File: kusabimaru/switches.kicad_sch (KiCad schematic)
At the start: 148 parts

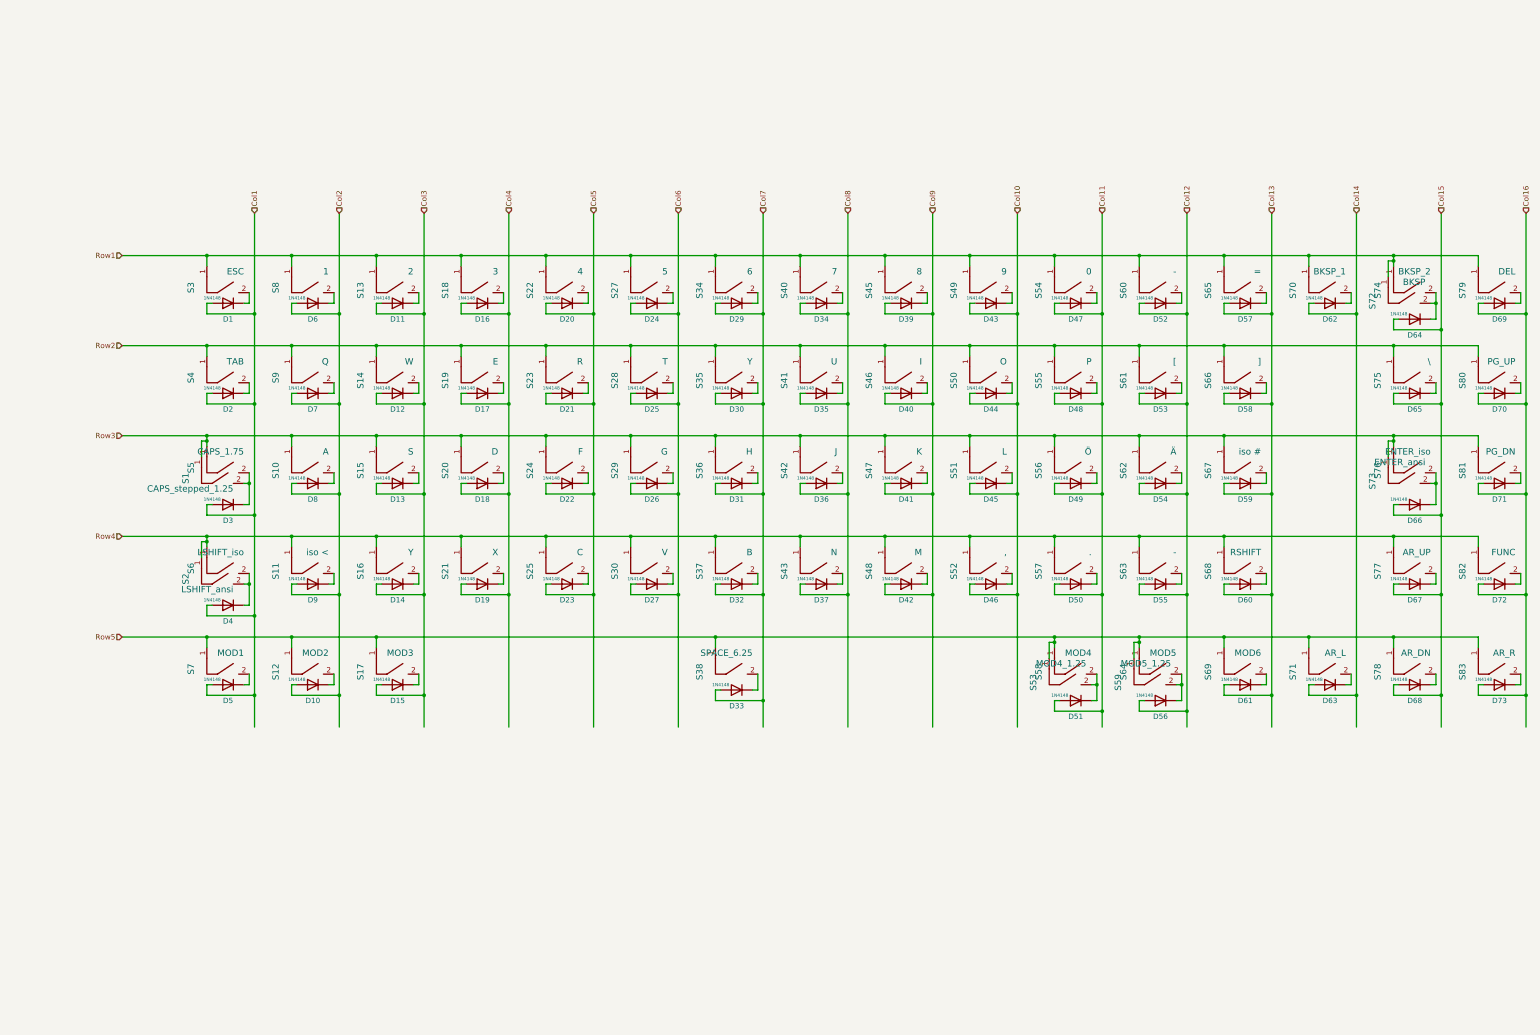
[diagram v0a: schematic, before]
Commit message: Changed schematic and PCB layout for kuro65. Routing of PCB is incomplete.
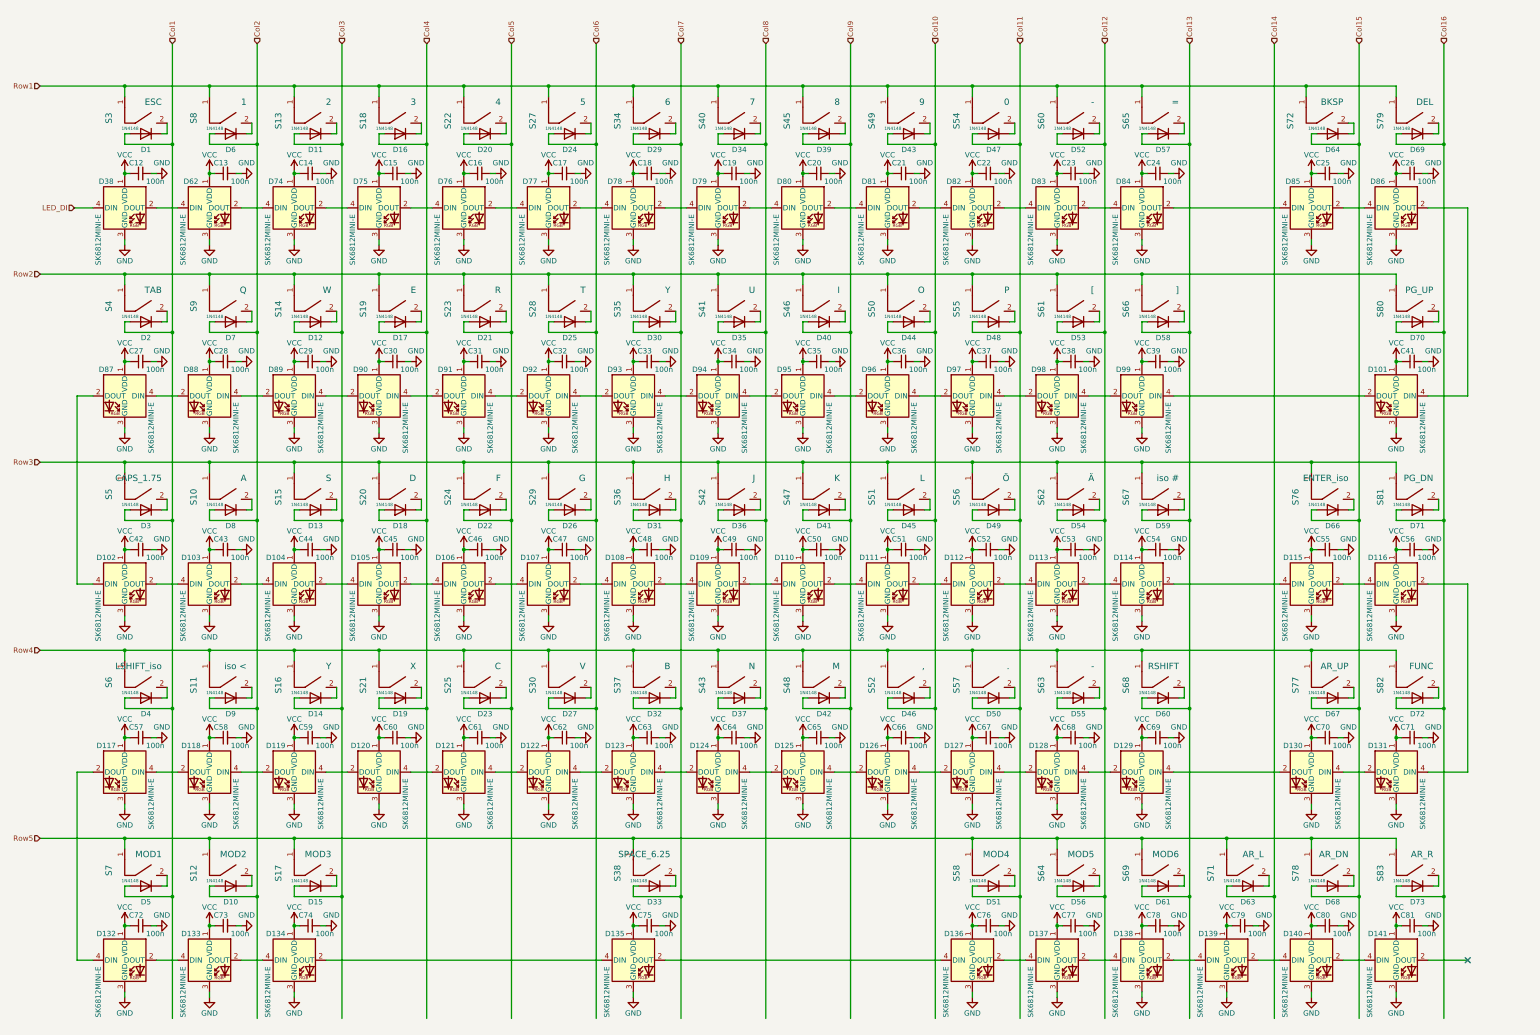
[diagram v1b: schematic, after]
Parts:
- removed D62, D65: 1N4148, Diode_SMD:D_SOD-323_HandSoldering, symbol Device:D
- removed S1: CAPS_stepped_1.25, keyswitches:Kailh_socket_only_MX_1.25u, symbol mx1a-simple:MX1A
- removed S2: LSHIFT_ansi, keyswitches:Kailh_socket_only_MX_2.25u, symbol mx1a-simple:MX1A
- removed S53: MOD4_1.25, keyswitches:Kailh_socket_only_MX_1.25u, symbol mx1a-simple:MX1A
- removed S59: MOD5_1.25, keyswitches:Kailh_socket_only_MX_1.25u, symbol mx1a-simple:MX1A
- removed S70: BKSP_1, keyswitches:Kailh_socket_only_MX_1u, symbol mx1a-simple:MX1A
- removed S73: ENTER_ansi, keyswitches:Kailh_socket_only_MX_2.25u, symbol mx1a-simple:MX1A
- removed S74: BKSP_2, keyswitches:Kailh_socket_only_MX_1u, symbol mx1a-simple:MX1A
- removed S75: \, keyswitches:Kailh_socket_only_MX_1.5u, symbol mx1a-simple:MX1A
- added C12, C13, C14, C15, C16, C17, C18, C19, C20, C21, C22, C23, C24, C25, C26, C27, C28, C29, C30, C31, C32, C33, C34, C35, C36, C37, C38, C39, C41, C42, C43, C44, C45, C46, C47, C48, C49, C50, C51, C52, C53, C54, C55, C56, C57, C58, C59, C60, C61, C62, C63, C64, C65, C66, C67, C68, C69, C70, C71, C72, C73, C74, C75, C76, C77, C78, C79, C80, C81: 100n, Capacitor_SMD:C_0603_1608Metric_Pad1.08x0.95mm_HandSolder, symbol Device:C_Small
- added D101, D102, D103, D104, D105, D106, D107, D108, D109, D110, D111, D112, D113, D114, D115, D116, D117, D118, D119, D120, D121, D122, D123, D124, D125, D126, D127, D128, D129, D130, D131, D132, D133, D134, D135, D136, D137, D138, D139, D140, D141, D38, D62, D74, D75, D76, D77, D78, D79, D80, D81, D82, D83, D84, D85, D86, D87, D88, D89, D90, D91, D92, D93, D94, D95, D96, D97, D98, D99: SK6812MINI-E, TM_leds:SK6812_MINI_E_small_cutout, symbol tm_leds:SK6812MINI-E
- D1, D10, D11, D12, D13, D14, D15, D16, D17, D18, D19, D2, D20, D21, D22, D23, D24, D25, D26, D27, D29, D3, D30, D31, D32, D33, D34, D35, D36, D37, D39, D4, D40, D41, D42, D43, D44, D45, D46, D47, D48, D49, D5, D50, D51, D52, D53, D54, D55, D56, D57, D58, D59, D6, D60, D61, D63, D64, D66, D67, D68, D69, D7, D70, D71, D72, D73, D8, D9: footprint Diode_SMD:D_SOD-323_HandSoldering -> Diode_SMD:D_SOD-123
- S10, S11, S13, S14, S15, S16, S18, S19, S20, S21, S22, S23, S24, S25, S27, S28, S29, S30, S34, S35, S36, S37, S40, S41, S42, S43, S45, S46, S47, S48, S49, S50, S51, S52, S54, S55, S56, S57, S58, S60, S61, S62, S63, S64, S65, S66, S67, S69, S71, S77, S78, S79, S80, S81, S82, S83, S9: footprint keyswitches:Kailh_socket_only_MX_1u -> keyswitches:Kailh_socket_only_MX_smd_1u
- S3, S8: footprint keyswitches:Kailh_socket_MX_1u -> keyswitches:Kailh_socket_only_MX_smd_1u
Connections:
- new net: D84.2 (DOUT), D85.4 (DIN)
- new net: D83.2 (DOUT), D84.4 (DIN)
- new net: D140.2 (DOUT), D141.4 (DIN)
- new net: D139.2 (DOUT), D140.4 (DIN)
- new net: D80.2 (DOUT), D81.4 (DIN)
- new net: D79.2 (DOUT), D80.4 (DIN)
- new net: D91.4 (DIN), D92.2 (DOUT)
- new net: D92.4 (DIN), D93.2 (DOUT)
- new net: D78.2 (DOUT), D79.4 (DIN)
- new net: D76.2 (DOUT), D77.4 (DIN)
- new net: D75.2 (DOUT), D76.4 (DIN)
- new net: D74.2 (DOUT), D75.4 (DIN)
- new net: D62.2 (DOUT), D74.4 (DIN)
- new net: D77.2 (DOUT), D78.4 (DIN)
- new net: D82.2 (DOUT), D83.4 (DIN)
- new net: D111.2 (DOUT), D112.4 (DIN)
- new net: D110.2 (DOUT), D111.4 (DIN)
- new net: D95.4 (DIN), D96.2 (DOUT)
- new net: D96.4 (DIN), D97.2 (DOUT)
- new net: D81.2 (DOUT), D82.4 (DIN)
- new net: D127.4 (DIN), D128.2 (DOUT)
- new net: D128.4 (DIN), D129.2 (DOUT)
- new net: D89.4 (DIN), D90.2 (DOUT)
- new net: D90.4 (DIN), D91.2 (DOUT)
- new net: D87.4 (DIN), D88.2 (DOUT)
- new net: D88.4 (DIN), D89.2 (DOUT)
- new net: D117.4 (DIN), D118.2 (DOUT)
- new net: D118.4 (DIN), D119.2 (DOUT)
- new net: D130.4 (DIN), D131.2 (DOUT)
- new net: D116.2 (DOUT), D131.4 (DIN)
- new net: D108.2 (DOUT), D109.4 (DIN)
- new net: D107.2 (DOUT), D108.4 (DIN)
- new net: D109.2 (DOUT), D110.4 (DIN)
- new net: D101.2 (DOUT), D99.4 (DIN)
- new net: D101.4 (DIN), D86.2 (DOUT)
- new net: D106.2 (DOUT), D107.4 (DIN)
- new net: D85.2 (DOUT), D86.4 (DIN)
- new net: D126.4 (DIN), D127.2 (DOUT)
- new net: D105.2 (DOUT), D106.4 (DIN)
- new net: D135.2 (DOUT), D136.4 (DIN)
- new net: D134.2 (DOUT), D135.4 (DIN)
- new net: D114.2 (DOUT), D115.4 (DIN)
- new net: D113.2 (DOUT), D114.4 (DIN)
- new net: D125.4 (DIN), D126.2 (DOUT)
- new net: D137.2 (DOUT), D138.4 (DIN)
- new net: D136.2 (DOUT), D137.4 (DIN)
- new net: D138.2 (DOUT), D139.4 (DIN)
- new net: D121.4 (DIN), D122.2 (DOUT)
- new net: D122.4 (DIN), D123.2 (DOUT)
- new net: D112.2 (DOUT), D113.4 (DIN)
- new net: D104.2 (DOUT), D105.4 (DIN)
- new net: D103.2 (DOUT), D104.4 (DIN)
- new net: D97.4 (DIN), D98.2 (DOUT)
- new net: D98.4 (DIN), D99.2 (DOUT)
- new net: D115.2 (DOUT), D116.4 (DIN)
- new net: D119.4 (DIN), D120.2 (DOUT)
- new net: D120.4 (DIN), D121.2 (DOUT)
- new net: D133.2 (DOUT), D134.4 (DIN)
- new net: D132.2 (DOUT), D133.4 (DIN)
- new net: D102.4 (DIN), D87.2 (DOUT)
- new net: D94.4 (DIN), D95.2 (DOUT)
- new net: D129.4 (DIN), D130.2 (DOUT)
- new net: D38.2 (DOUT), D62.4 (DIN)
- new net: D102.2 (DOUT), D103.4 (DIN)
- new net: D117.2 (DOUT), D132.4 (DIN)
- new net: D123.4 (DIN), D124.2 (DOUT)
- new net: D93.4 (DIN), D94.2 (DOUT)
- new net: D124.4 (DIN), D125.2 (DOUT)
- new net GND: C12.2, C13.2, C14.2, C15.2, C16.2, C17.2, C18.2, C19.2, C20.2, C21.2, C22.2, C23.2, C24.2, C25.2, C26.2, C27.2, C28.2, C29.2, C30.2, C31.2, C32.2, C33.2, C34.2, C35.2, C36.2, C37.2, C38.2, C39.2, C41.2, C42.2, C43.2, C44.2, C45.2, C46.2, C47.2, C48.2, C49.2, C50.2, C51.2, C52.2, C53.2, C54.2, C55.2, C56.2, C57.2, C58.2, C59.2, C60.2, C61.2, C62.2, C63.2, C64.2, C65.2, C66.2, C67.2, C68.2, C69.2, C70.2, C71.2, C72.2, C73.2, C74.2, C75.2, C76.2, C77.2, C78.2, C79.2, C80.2, C81.2, D101.3 (GND), D102.3 (GND), D103.3 (GND), D104.3 (GND), D105.3 (GND), D106.3 (GND), D107.3 (GND), D108.3 (GND), D109.3 (GND), D110.3 (GND), D111.3 (GND), D112.3 (GND), D113.3 (GND), D114.3 (GND), D115.3 (GND), D116.3 (GND), D117.3 (GND), D118.3 (GND), D119.3 (GND), D120.3 (GND), D121.3 (GND), D122.3 (GND), D123.3 (GND), D124.3 (GND), D125.3 (GND), D126.3 (GND), D127.3 (GND), D128.3 (GND), D129.3 (GND), D130.3 (GND), D131.3 (GND), D132.3 (GND), D133.3 (GND), D134.3 (GND), D135.3 (GND), D136.3 (GND), D137.3 (GND), D138.3 (GND), D139.3 (GND), D140.3 (GND), D141.3 (GND), D38.3 (GND), D62.3 (GND), D74.3 (GND), D75.3 (GND), D76.3 (GND), D77.3 (GND), D78.3 (GND), D79.3 (GND), D80.3 (GND), D81.3 (GND), D82.3 (GND), D83.3 (GND), D84.3 (GND), D85.3 (GND), D86.3 (GND), D87.3 (GND), D88.3 (GND), D89.3 (GND), D90.3 (GND), D91.3 (GND), D92.3 (GND), D93.3 (GND), D94.3 (GND), D95.3 (GND), D96.3 (GND), D97.3 (GND), D98.3 (GND), D99.3 (GND)
- new net LED_DI: D38.4 (DIN)
- new net VCC: C12.1, C13.1, C14.1, C15.1, C16.1, C17.1, C18.1, C19.1, C20.1, C21.1, C22.1, C23.1, C24.1, C25.1, C26.1, C27.1, C28.1, C29.1, C30.1, C31.1, C32.1, C33.1, C34.1, C35.1, C36.1, C37.1, C38.1, C39.1, C41.1, C42.1, C43.1, C44.1, C45.1, C46.1, C47.1, C48.1, C49.1, C50.1, C51.1, C52.1, C53.1, C54.1, C55.1, C56.1, C57.1, C58.1, C59.1, C60.1, C61.1, C62.1, C63.1, C64.1, C65.1, C66.1, C67.1, C68.1, C69.1, C70.1, C71.1, C72.1, C73.1, C74.1, C75.1, C76.1, C77.1, C78.1, C79.1, C80.1, C81.1, D101.1 (VDD), D102.1 (VDD), D103.1 (VDD), D104.1 (VDD), D105.1 (VDD), D106.1 (VDD), D107.1 (VDD), D108.1 (VDD), D109.1 (VDD), D110.1 (VDD), D111.1 (VDD), D112.1 (VDD), D113.1 (VDD), D114.1 (VDD), D115.1 (VDD), D116.1 (VDD), D117.1 (VDD), D118.1 (VDD), D119.1 (VDD), D120.1 (VDD), D121.1 (VDD), D122.1 (VDD), D123.1 (VDD), D124.1 (VDD), D125.1 (VDD), D126.1 (VDD), D127.1 (VDD), D128.1 (VDD), D129.1 (VDD), D130.1 (VDD), D131.1 (VDD), D132.1 (VDD), D133.1 (VDD), D134.1 (VDD), D135.1 (VDD), D136.1 (VDD), D137.1 (VDD), D138.1 (VDD), D139.1 (VDD), D140.1 (VDD), D141.1 (VDD), D38.1 (VDD), D62.1 (VDD), D74.1 (VDD), D75.1 (VDD), D76.1 (VDD), D77.1 (VDD), D78.1 (VDD), D79.1 (VDD), D80.1 (VDD), D81.1 (VDD), D82.1 (VDD), D83.1 (VDD), D84.1 (VDD), D85.1 (VDD), D86.1 (VDD), D87.1 (VDD), D88.1 (VDD), D89.1 (VDD), D90.1 (VDD), D91.1 (VDD), D92.1 (VDD), D93.1 (VDD), D94.1 (VDD), D95.1 (VDD), D96.1 (VDD), D97.1 (VDD), D98.1 (VDD), D99.1 (VDD)
- no-connect marks 0 -> 1
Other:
- moved on the sheet: D1, D10, D11, D12, D13, D14, D15, D16, D17, D18, D19, D2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

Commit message: Updates on PCB layout. Placement of LED components corrected.
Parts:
- S12, S17, S6, S7: footprint keyswitches:Kailh_socket_only_MX_1.25u -> keyswitches:Kailh_socket_only_MX_smd_1.25u
- S38: footprint keyswitches:Kailh_socket_only_MX_6.25u -> keyswitches:Kailh_socket_only_MX_smd_6.25u
- S4: footprint keyswitches:Kailh_socket_only_MX_1.5u -> keyswitches:Kailh_socket_only_MX_smd_1.5u
- S5, S68: footprint keyswitches:Kailh_socket_only_MX_1.75u -> keyswitches:Kailh_socket_only_MX_smd_1.75u
- S72: footprint keyswitches:Kailh_socket_only_MX_2u -> keyswitches:Kailh_socket_only_MX_smd_2u
- S76: footprint keyswitches:Kailh_socket_only_MX_iso_enter -> keyswitches:Kailh_socket_only_MX_smd_iso_enter
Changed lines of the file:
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@@
       (effects (font (size 1.524 1.524)) (justify right))
     )
-    (property "Footprint" "keyswitches:Kailh_socket_only_MX_1.5u" (id 2) (at 45.085 86.995 0)
+    (property "Footprint" "keyswitches:Kailh_socket_only_MX_smd_1.5u" (id 2) (at 45.085 86.995 0)
       (effects (font (size 1.27 1.27)) hide)
     )
@@
       (effects (font (size 1.524 1.524)) (justify right))
     )
-    (property "Footprint" "keyswitches:Kailh_socket_only_MX_1.75u" (id 2) (at 45.085 132.08 0)
+    (property "Footprint" "keyswitches:Kailh_socket_only_MX_smd_1.75u" (id 2) (at 45.085 132.08 0)
       (effects (font (size 1.27 1.27)) hide)
     )
@@
       (effects (font (size 1.524 1.524)) (justify right))
     )
-    (property "Footprint" "keyswitches:Kailh_socket_only_MX_iso_enter" (id 2) (at 329.565 132.08 0)
+    (property "Footprint" "keyswitches:Kailh_socket_only_MX_smd_iso_enter" (id 2) (at 329.565 132.08 0)
       (effects (font (size 1.27 1.27)) hide)
     )
@@
       (effects (font (size 1.524 1.524)) (justify right))
     )
-    (property "Footprint" "keyswitches:Kailh_socket_only_MX_1.25u" (id 2) (at 45.085 177.165 0)
+    (property "Footprint" "keyswitches:Kailh_socket_only_MX_smd_1.25u" (id 2) (at 45.085 177.165 0)
       (effects (font (size 1.27 1.27)) hide)
     )
@@
       (effects (font (size 1.524 1.524)) (justify right))
     )
-    (property "Footprint" "keyswitches:Kailh_socket_only_MX_1.75u" (id 2) (at 288.925 177.165 0)
+    (property "Footprint" "keyswitches:Kailh_socket_only_MX_smd_1.75u" (id 2) (at 288.925 177.165 0)
       (effects (font (size 1.27 1.27)) hide)
     )
@@
       (effects (font (size 1.524 1.524)) (justify right))
     )
-    (property "Footprint" "keyswitches:Kailh_socket_only_MX_1.25u" (id 2) (at 45.085 222.25 0)
+    (property "Footprint" "keyswitches:Kailh_socket_only_MX_smd_1.25u" (id 2) (at 45.085 222.25 0)
       (effects (font (size 1.27 1.27)) hide)
     )
@@
       (effects (font (size 1.524 1.524)) (justify right))
     )
-    (property "Footprint" "keyswitches:Kailh_socket_only_MX_1.25u" (id 2) (at 65.405 222.25 0)
+    (property "Footprint" "keyswitches:Kailh_socket_only_MX_smd_1.25u" (id 2) (at 65.405 222.25 0)
       (effects (font (size 1.27 1.27)) hide)
     )
@@
       (effects (font (size 1.524 1.524)) (justify right))
     )
-    (property "Footprint" "keyswitches:Kailh_socket_only_MX_1.25u" (id 2) (at 85.725 222.25 0)
+    (property "Footprint" "keyswitches:Kailh_socket_only_MX_smd_1.25u" (id 2) (at 85.725 222.25 0)
       (effects (font (size 1.27 1.27)) hide)
     )
@@
       (effects (font (size 1.524 1.524)) (justify right))
     )
-    (property "Footprint" "keyswitches:Kailh_socket_only_MX_6.25u" (id 2) (at 167.005 222.25 0)
+    (property "Footprint" "keyswitches:Kailh_socket_only_MX_smd_6.25u" (id 2) (at 167.005 222.25 0)
       (effects (font (size 1.27 1.27)) hide)
     )
@@
       (effects (font (size 1.524 1.524)) (justify right))
     )
-    (property "Footprint" "keyswitches:Kailh_socket_only_MX_2u" (id 2) (at 328.295 41.91 0)
-      (effects (font (size 1.27 1.27)) hide)
-    )
+    (property "Footprint" "keyswitches:Kailh_socket_only_MX_smd_2u" (id 2) (at 328.295 41.91 0)
+      (effects (font (size 1.27 1.27)) hide)
+    )

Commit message: Updates in routed PCB.
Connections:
- net LED_DI: now also D135.4 (DIN); no longer D38.4 (DIN)
- net at D141.2 (DOUT): now also D131.4 (DIN)
- net at D118.2 (DOUT): now also D134.4 (DIN); no longer D117.4 (DIN)
- net at D116.2 (DOUT): now also D101.4 (DIN); no longer D131.4 (DIN)
- net at D86.2 (DOUT): no longer D101.4 (DIN)
- net at D134.2 (DOUT): now also D133.4 (DIN); no longer D135.4 (DIN)
- net at D133.2 (DOUT): now also D132.4 (DIN); no longer D134.4 (DIN)
- net at D132.2 (DOUT): now also D117.4 (DIN); no longer D133.4 (DIN)
- net at D87.2 (DOUT): now also D38.4 (DIN); no longer D102.4 (DIN)
- net at D117.2 (DOUT): now also D102.4 (DIN); no longer D132.4 (DIN)

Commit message: Updates on PCB, schematic and submodules.
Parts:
- S12: footprint keyswitches:Kailh_socket_only_MX_smd_1.25u -> keyswitches:Kailh_socket_only_MX_smd_1.25u_clipped_pin
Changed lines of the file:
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@@
       (effects (font (size 1.524 1.524)) (justify right))
     )
-    (property "Footprint" "keyswitches:Kailh_socket_only_MX_smd_1.25u" (id 2) (at 65.405 222.25 0)
+    (property "Footprint" "keyswitches:Kailh_socket_only_MX_smd_1.25u_clipped_pin" (id 2) (at 65.405 222.25 0)
       (effects (font (size 1.27 1.27)) hide)
     )
